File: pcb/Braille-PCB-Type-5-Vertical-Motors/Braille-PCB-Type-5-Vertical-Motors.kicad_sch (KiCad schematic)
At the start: 25 parts, among them J1 Screw_Terminal_01x02, J2 Screw_Terminal_01x02, J3 Screw_Terminal_01x02, J4 Conn_01x03, J5 Conn_01x02, J6 Conn_01x08, SW1 SW_Push, SW2 SW_Push, U1 RP2040-Zero

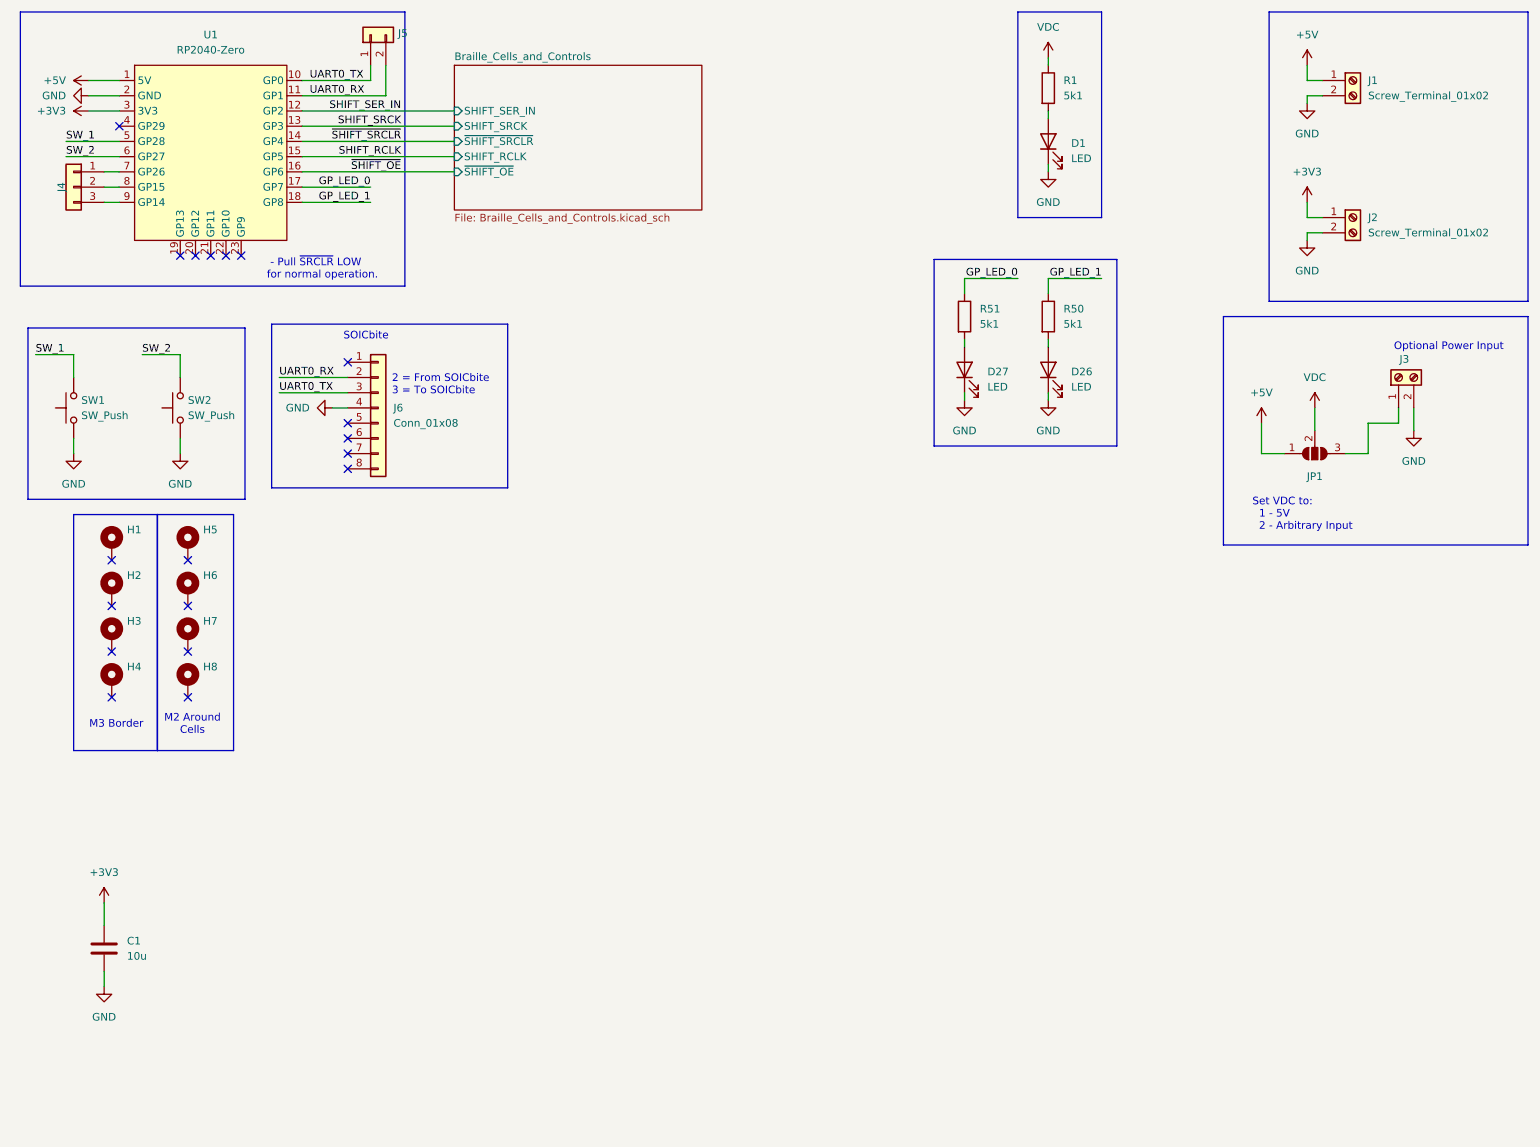
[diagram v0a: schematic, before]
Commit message: PCB: Update to have 3 motors, dimensioned layout template
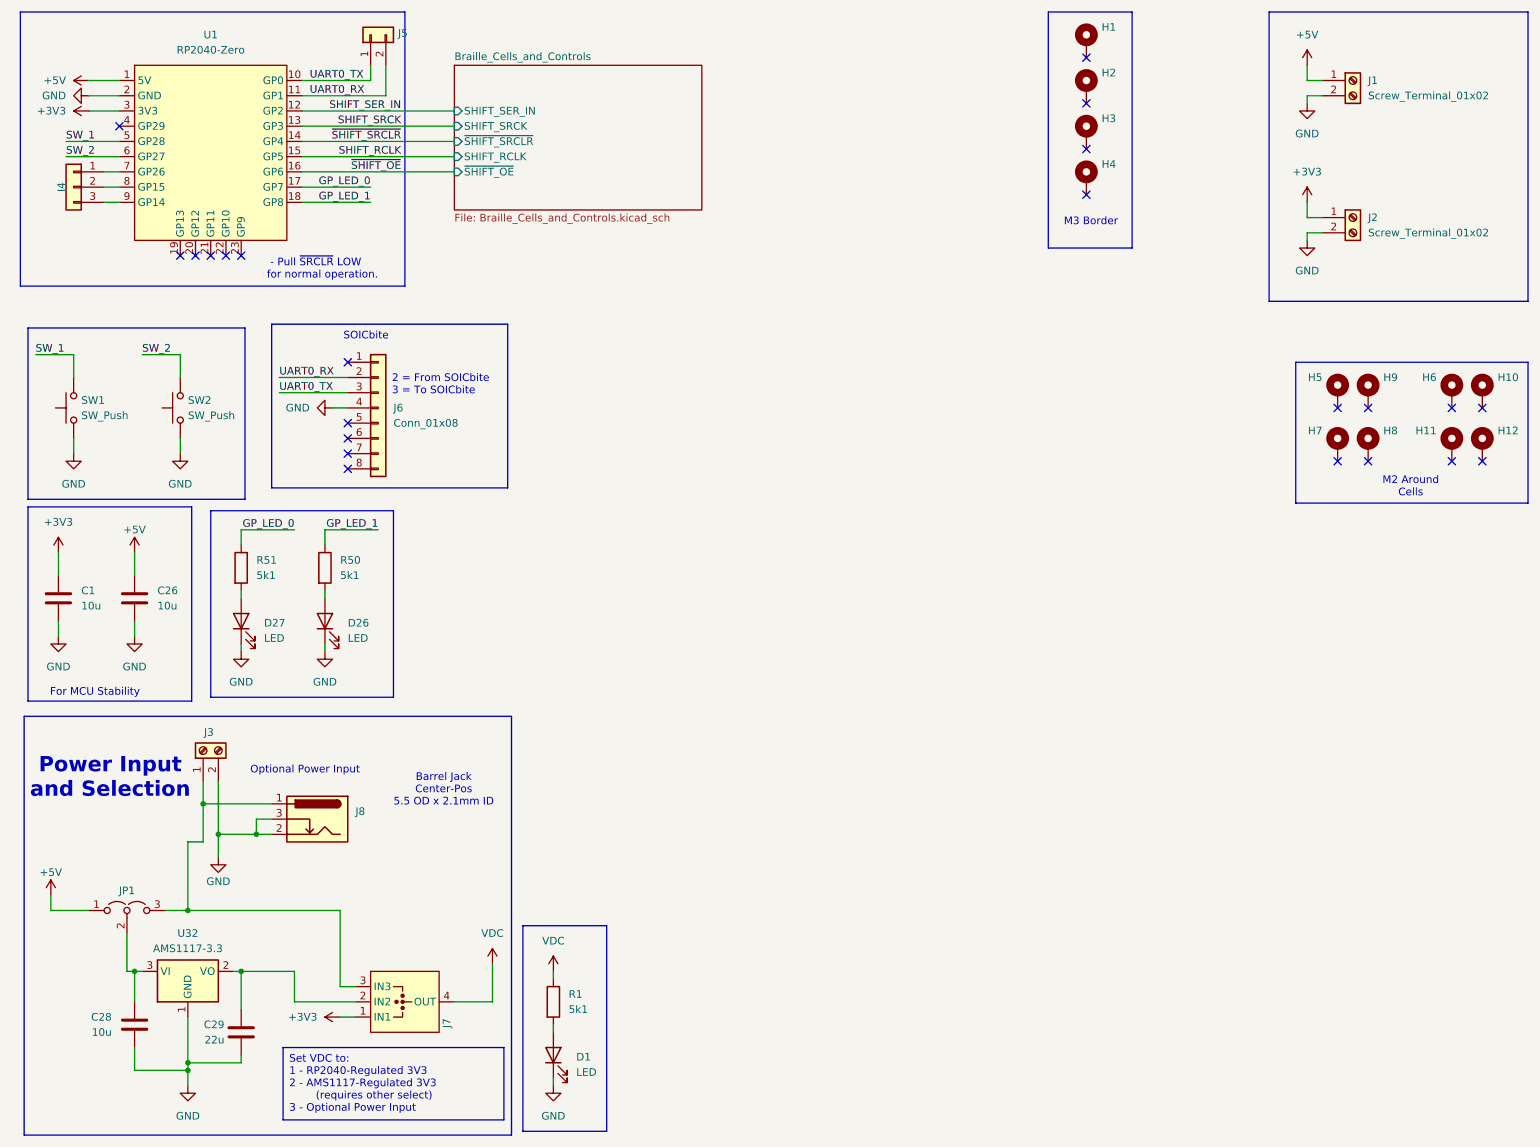
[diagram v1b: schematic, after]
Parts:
- removed JP1: SolderJumper_3_Open, Connector_PinHeader_2.54mm:PinHeader_1x03_P2.54mm_Vertical, symbol Jumper:SolderJumper_3_Open
- added C26, C28: 10u, Capacitor_SMD:C_1206_3216Metric_Pad1.33x1.80mm_HandSolder, symbol Device:C
- added C29: 22u, Capacitor_SMD:C_1206_3216Metric_Pad1.33x1.80mm_HandSolder, symbol Device:C
- added H10, H11, H12, H9: MountingHole_Pad, 00-project-footprints:Braille_Block_MountingHoles_M2_3x, symbol Mechanical:MountingHole_Pad
- added J7: Jumper-3-Way-Power, 00-project-footprints:Jumper-3-Way-2.54mm-Headers, symbol 00-project-symbols:Jumper-3-Way-Power
- added J8: Barrel_Jack_Switch, Connector_BarrelJack:BarrelJack_Horizontal, symbol Connector:Barrel_Jack_Switch
- added JP1: Jumper_3_Open, Connector_PinHeader_2.54mm:PinHeader_1x03_P2.54mm_Vertical, symbol Jumper:Jumper_3_Open
- added U32: AMS1117-3.3, Package_TO_SOT_SMD:SOT-223-3_TabPin2, symbol Regulator_Linear:AMS1117-3.3
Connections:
- net +3V3: now also J7.1 (IN1)
- net +5V: now also C26.1, JP1.1 (A)
- net GND: now also C26.2, C28.2, C29.2, J8.2, J8.3, U32.1 (GND)
- net VDC: now also J7.4 (OUT)
- net at J3.1 (Pin_1): now also J7.3 (IN3), J8.1, JP1.3 (B)
- new net: C29.1, J7.2 (IN2), U32.2 (VO)
- new net: C28.1, JP1.2 (C), U32.3 (VI)
- no-connect marks 19 -> 23
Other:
- note added: "Barrel Jack Center-Pos 5.5 OD x 2.1mm ID"
- note added: "For MCU Stability"
- note added: "Power Input and Selection"
- note removed: "Set VDC to: 1 - 5V 2 - Arbitrary Input"
- moved on the sheet: C1, D1, D26, D27, H1, H2, H3, H4, H5, H6, J3, R1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

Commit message: PCB WIP: Add motor shaft holes
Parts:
- D1, D26, D27: footprint LED_SMD:LED_1206_3216Metric_Pad1.42x1.75mm_HandSolder -> LED_SMD:LED_0603_1608Metric_Pad1.05x0.95mm_HandSolder
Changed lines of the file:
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@@
 			)
 		)
-		(property "Footprint" "LED_SMD:LED_1206_3216Metric_Pad1.42x1.75mm_HandSolder"
+		(property "Footprint" "LED_SMD:LED_0603_1608Metric_Pad1.05x0.95mm_HandSolder"
 			(at 50.8 115.57 0)
 			(effects
@@
 			)
 		)
-		(property "Footprint" "LED_SMD:LED_1206_3216Metric_Pad1.42x1.75mm_HandSolder"
+		(property "Footprint" "LED_SMD:LED_0603_1608Metric_Pad1.05x0.95mm_HandSolder"
 			(at 64.77 115.57 0)
 			(effects
@@
 			)
 		)
-		(property "Footprint" "LED_SMD:LED_1206_3216Metric_Pad1.42x1.75mm_HandSolder"
+		(property "Footprint" "LED_SMD:LED_0603_1608Metric_Pad1.05x0.95mm_HandSolder"
 			(at 102.87 187.96 0)
 			(effects

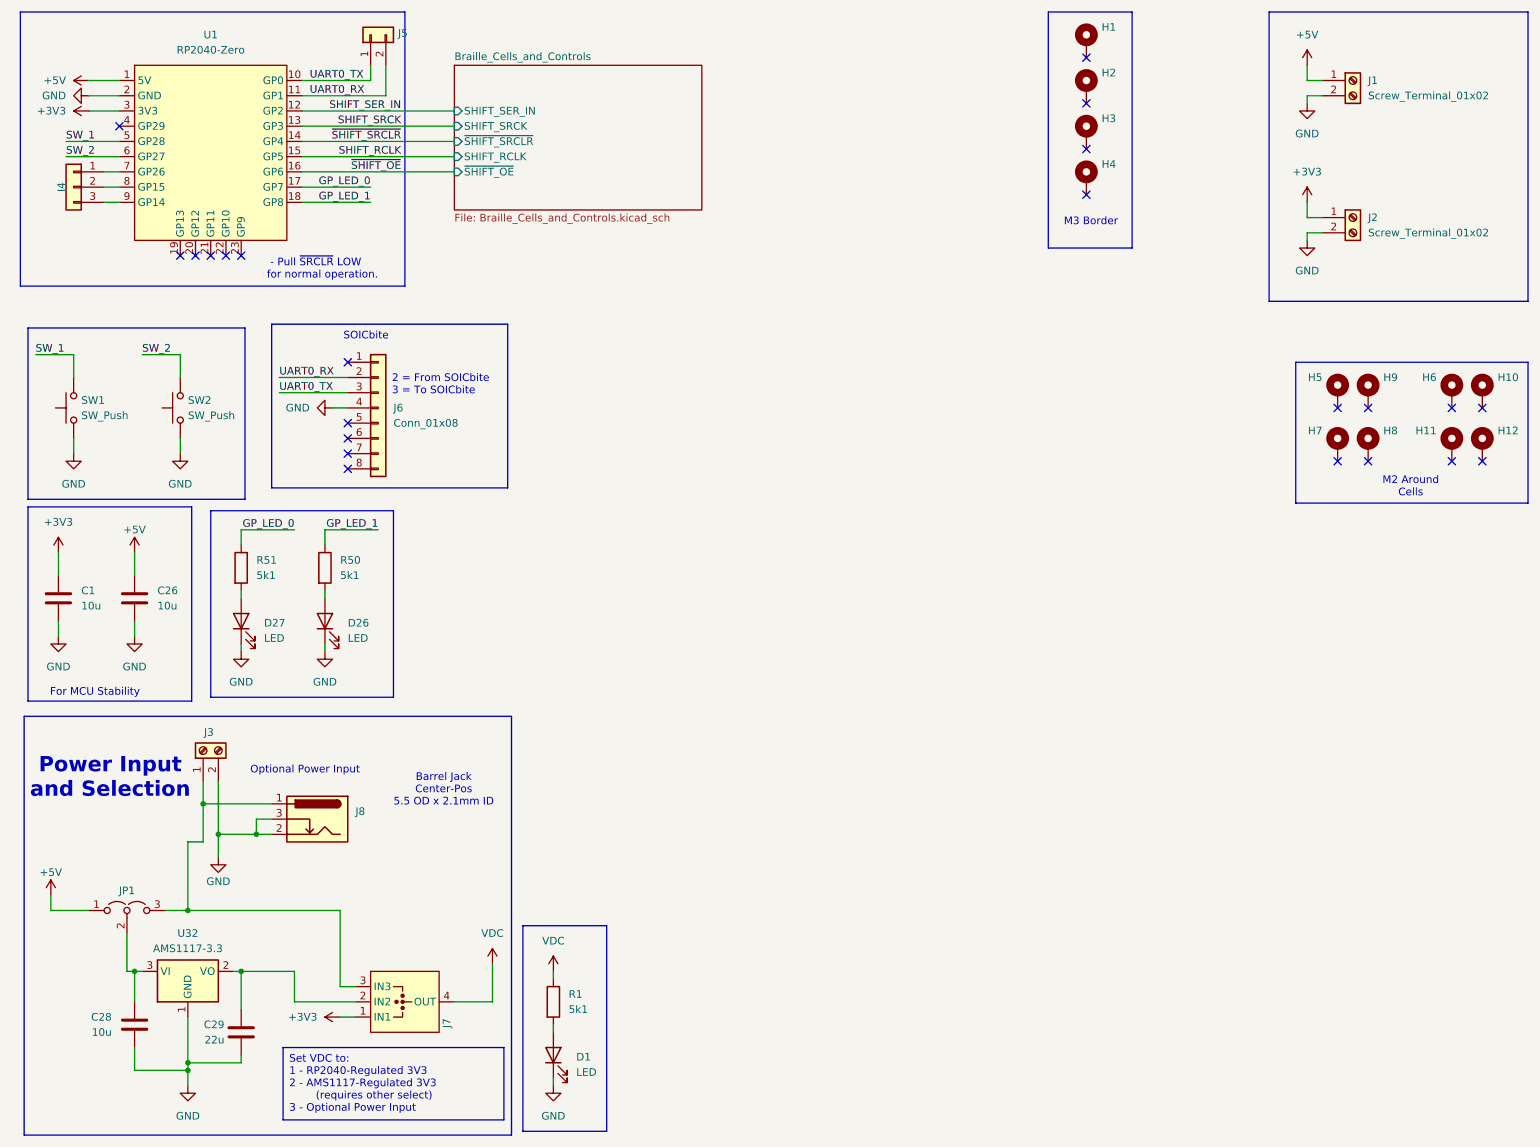
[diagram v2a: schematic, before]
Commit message: PCB: Add cross-PCB connectors
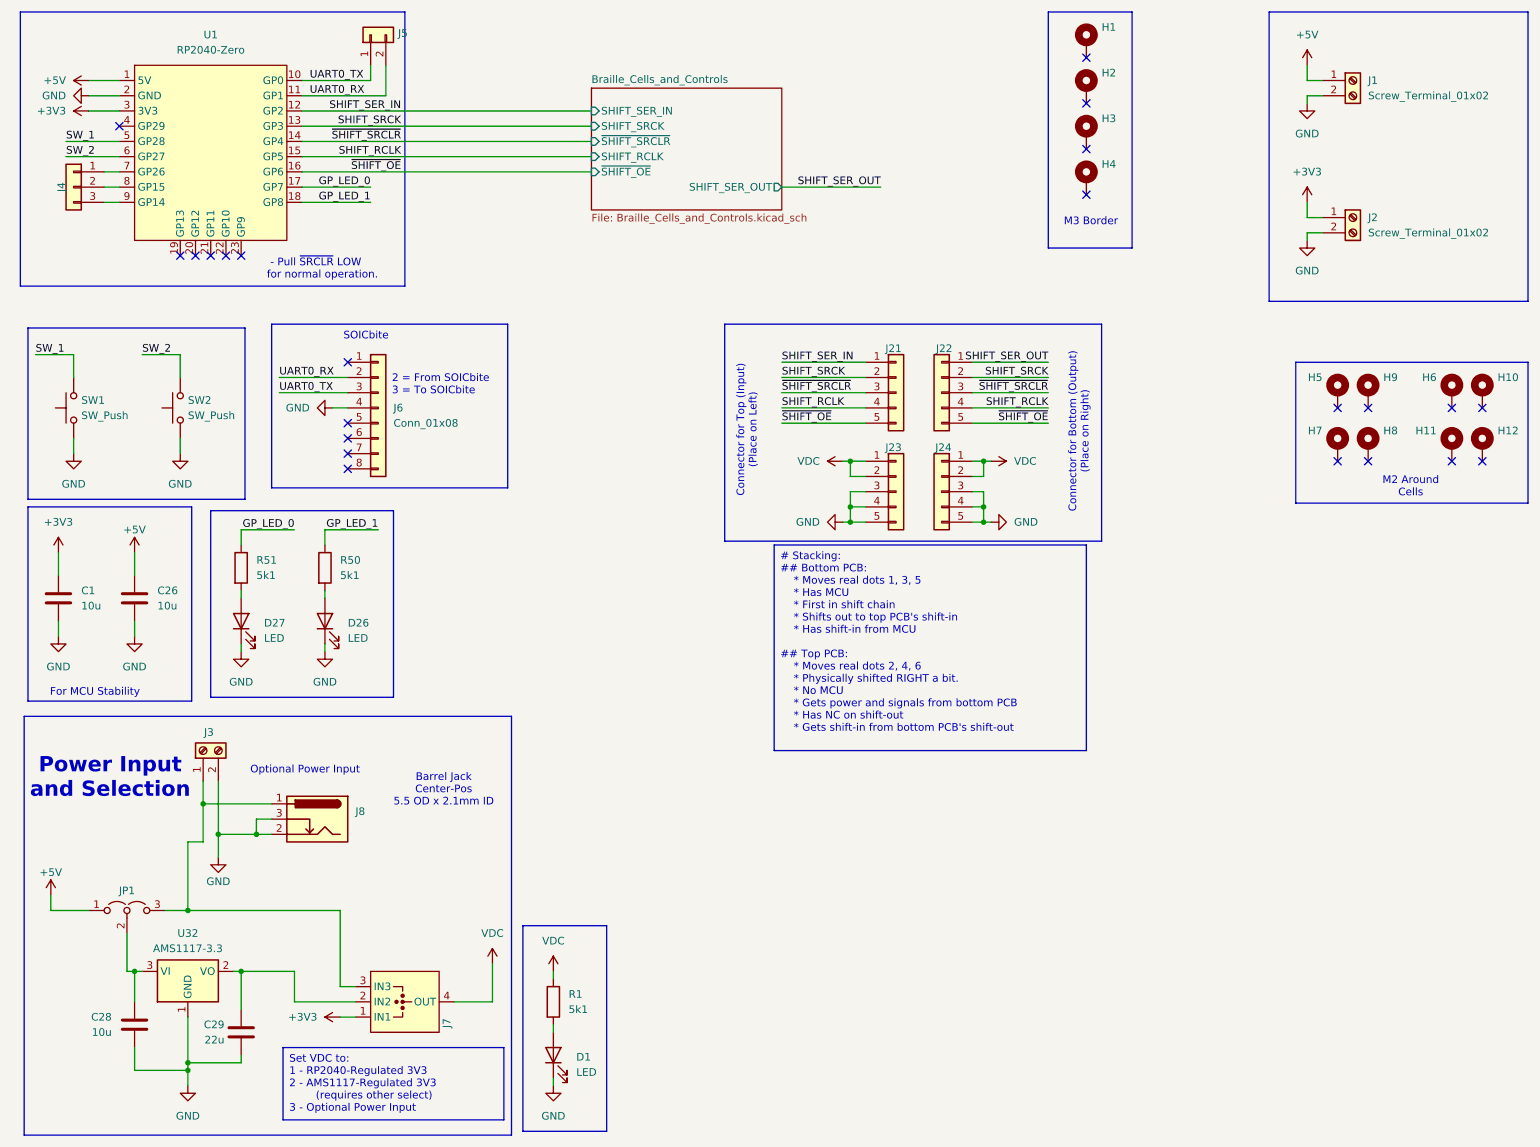
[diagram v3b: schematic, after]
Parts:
- added J21, J22, J23, J24: Conn_01x05, 00-project-footprints:PinHeader_1x05_P2.54mm_Vertical_Tight_Centered, symbol Connector_Generic:Conn_01x05
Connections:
- net GND: now also J23.3 (Pin_3), J23.4 (Pin_4), J23.5 (Pin_5), J24.3 (Pin_3), J24.4 (Pin_4), J24.5 (Pin_5)
- net SHIFT_RCLK: now also J21.4 (Pin_4), J22.4 (Pin_4)
- net SHIFT_SER_IN: now also J21.1 (Pin_1)
- net SHIFT_SRCK: now also J21.2 (Pin_2), J22.2 (Pin_2)
- net VDC: now also J23.1 (Pin_1), J23.2 (Pin_2), J24.1 (Pin_1), J24.2 (Pin_2)
- net ~{SHIFT_OE}: now also J21.5 (Pin_5), J22.5 (Pin_5)
- net ~{SHIFT_SRCLR}: now also J21.3 (Pin_3), J22.3 (Pin_3)
- new net SHIFT_SER_OUT: J22.1 (Pin_1)
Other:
- sheet Braille_Cells_and_Controls ports: added SHIFT_SER_OUT; removed none
- note added: "Connector for Bottom (Output) (Place on Right)"
- note added: "Connector for Top (Input) (Place on Left)"
